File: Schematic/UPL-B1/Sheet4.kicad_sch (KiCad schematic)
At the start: 61 parts, among them P40 TestPoint

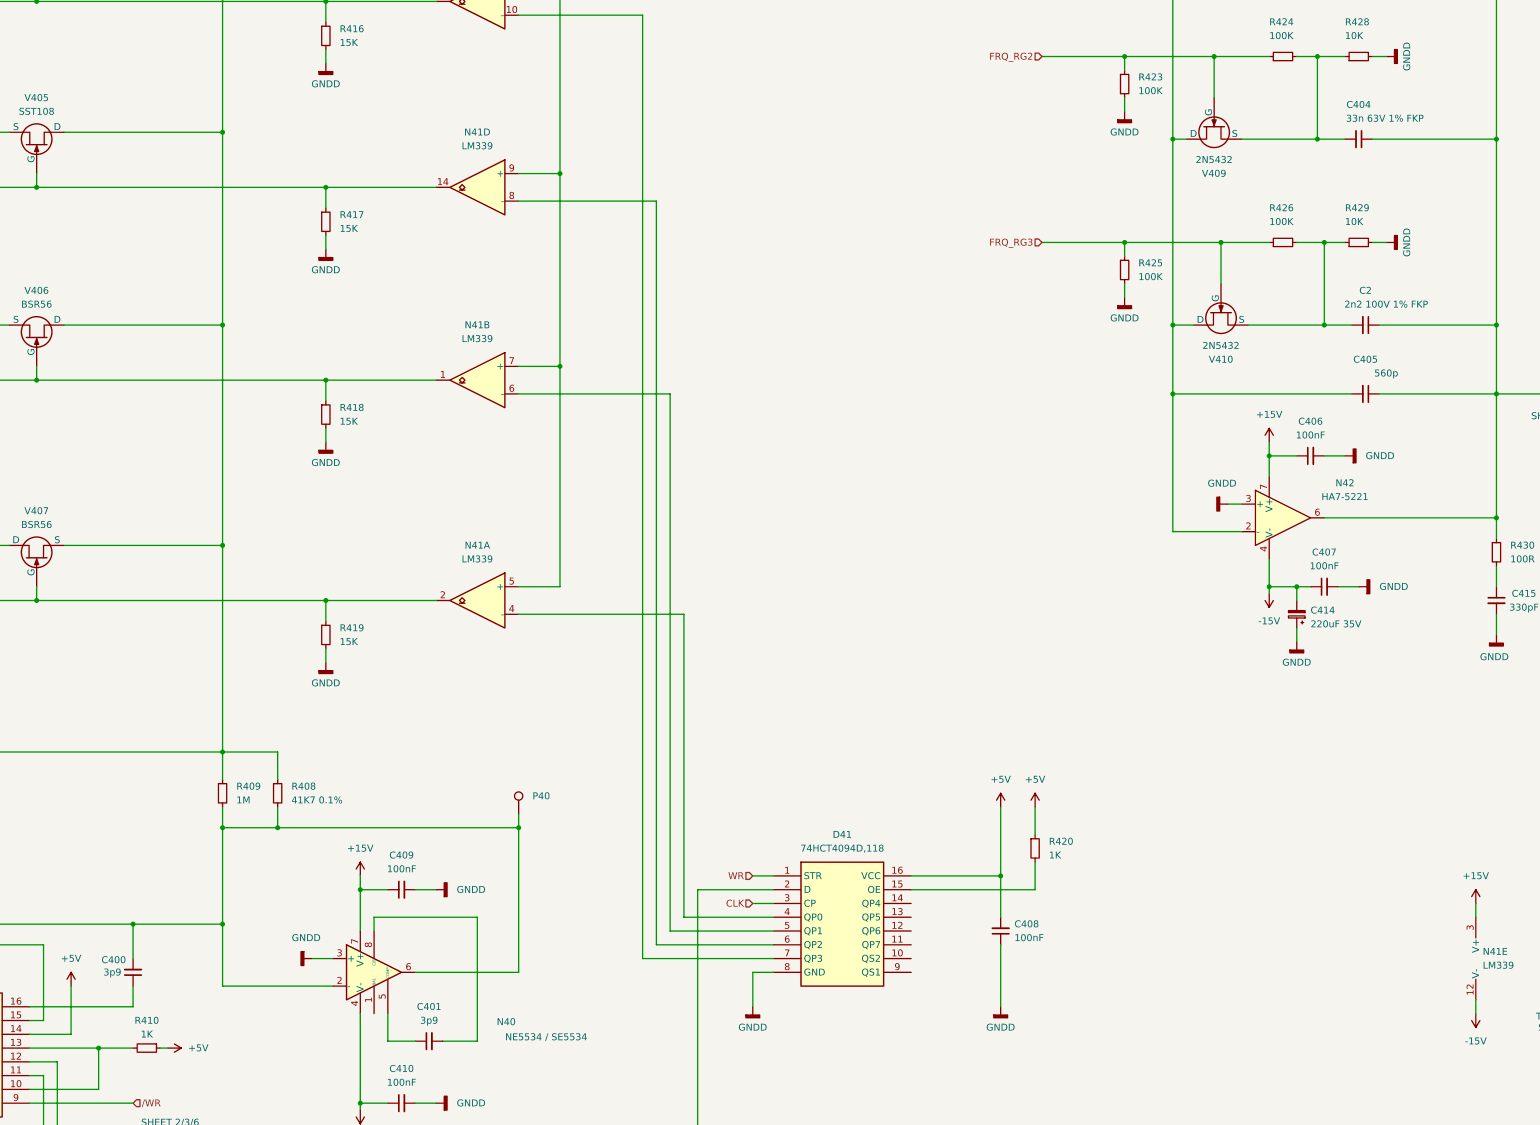
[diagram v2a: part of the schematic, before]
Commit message: Cleanup component names
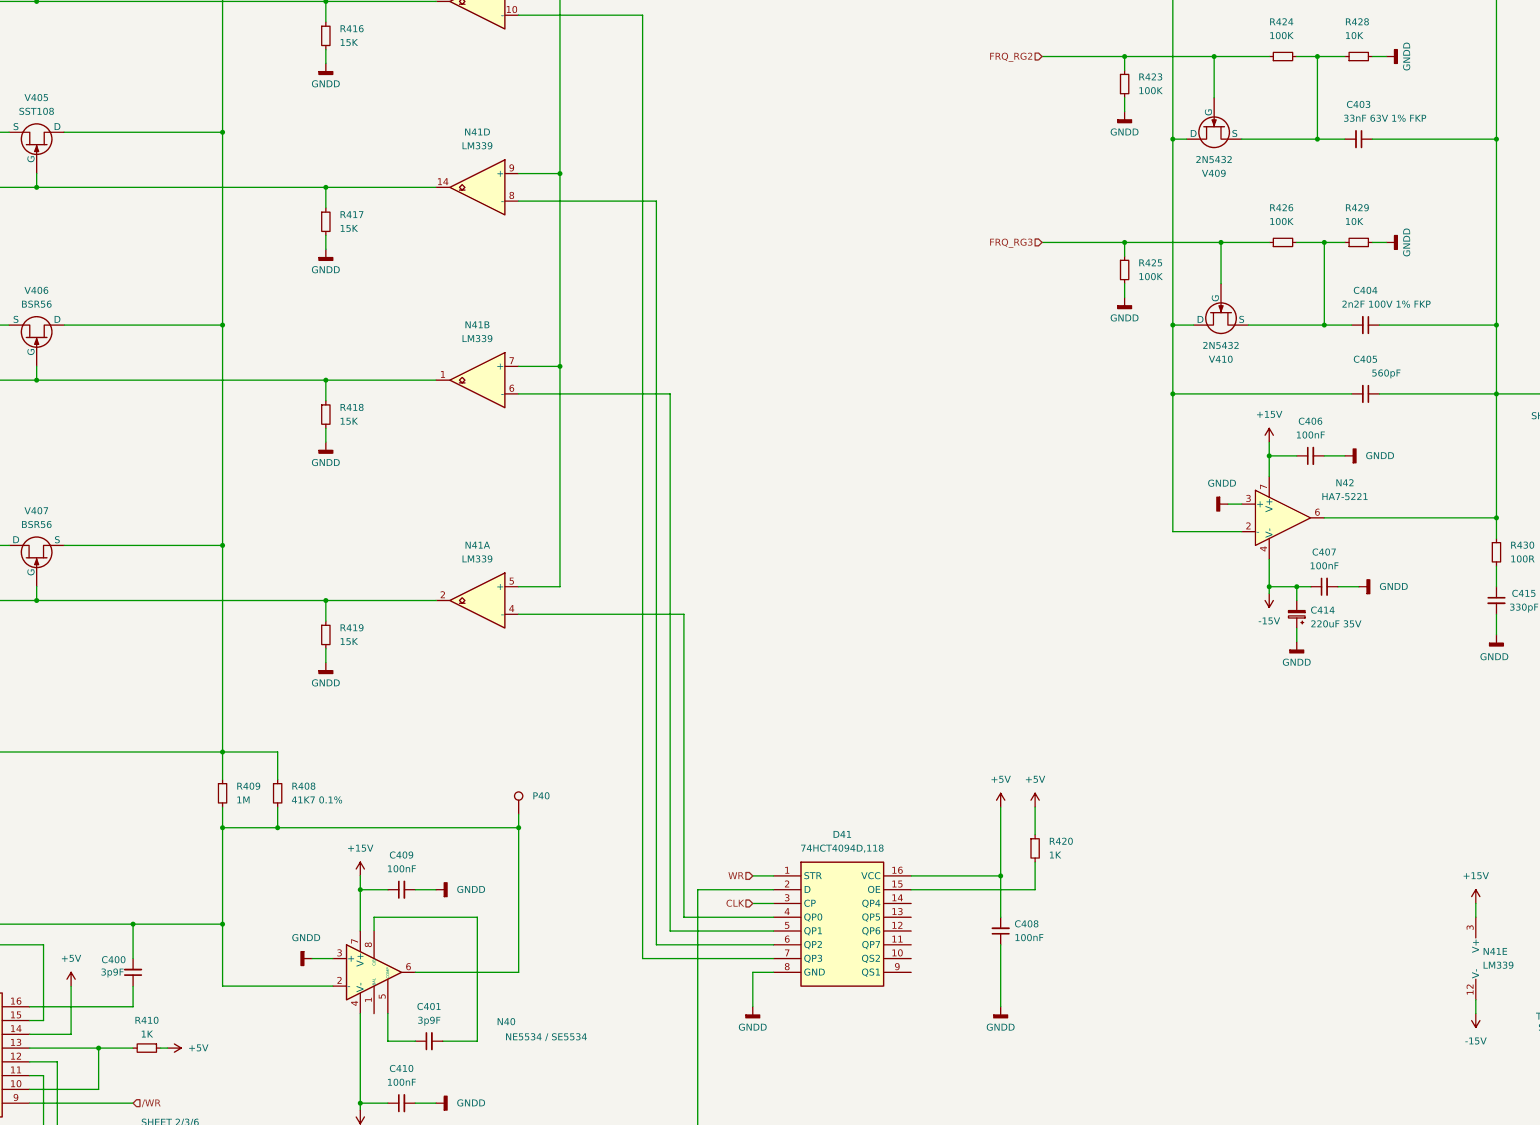
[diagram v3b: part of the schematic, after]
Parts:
- C400, C401: value 3p9 -> 3p9F
- C403: renamed from C404; value 33n 63V 1% FKP -> 33nF 63V 1% FKP
- C404: renamed from C2; value 2n2 100V 1% FKP -> 2n2F 100V 1% FKP
- C405: value 560p -> 560pF
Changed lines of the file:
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@@
 		(on_board yes)
 		(dnp no)
-		(property "Reference" "C404"
+		(property "Reference" "C403"
 			(at 354.3236 68.58 90)
 			(effects
@@
 			)
 		)
-		(property "Value" "33n 63V 1% FKP"
+		(property "Value" "33nF 63V 1% FKP"
 			(at 359.156 71.12 90)
 			(effects
@@
 			(project "UPL_B1"
 				(path "/812de09b-8b67-463d-bf96-bb3aeeb1ed8d/5c1faa4b-2306-4f0f-97e7-c76d1ee80adb"
-					(reference "C404")
+					(reference "C403")
 					(unit 1)
 				)
@@
 			)
 		)
-		(property "Value" "3p9"
+		(property "Value" "3p9F"
 			(at 182.8863 237.49 90)
 			(effects
@@
 			)
 		)
-		(property "Value" "3p9"
+		(property "Value" "3p9F"
 			(at 124.46 228.5937 0)
 			(effects
@@
 		(on_board yes)
 		(dnp no)
-		(property "Reference" "C2"
+		(property "Reference" "C404"
 			(at 355.5936 102.87 90)
 			(effects
@@
 			)
 		)
-		(property "Value" "2n2 100V 1% FKP"
+		(property "Value" "2n2F 100V 1% FKP"
 			(at 359.41 105.41 90)
 			(effects
@@
 			(project "UPL_B1"
 				(path "/812de09b-8b67-463d-bf96-bb3aeeb1ed8d/5c1faa4b-2306-4f0f-97e7-c76d1ee80adb"
-					(reference "C2")
+					(reference "C404")
 					(unit 1)
 				)
@@
 			)
 		)
-		(property "Value" "560p"
+		(property "Value" "560pF"
 			(at 359.41 118.11 90)
 			(effects

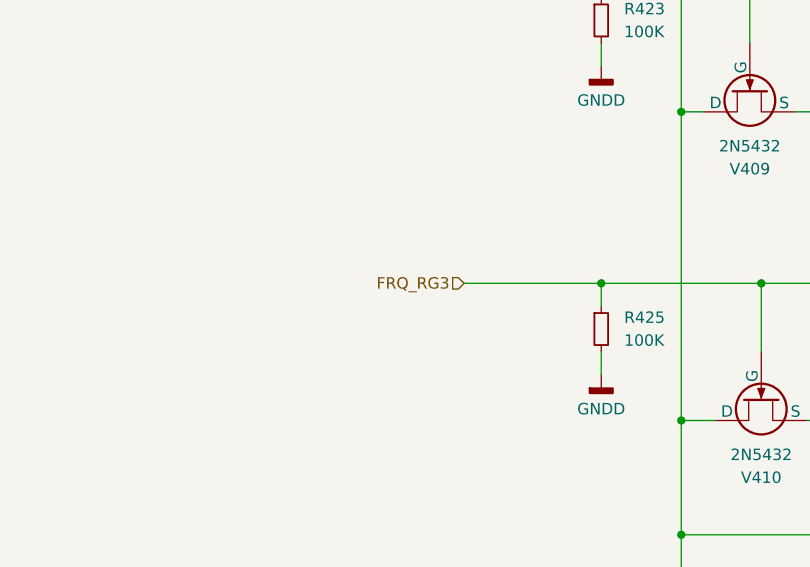
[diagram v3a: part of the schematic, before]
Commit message: Redraw block diagram as vector art. Add more links in hierarchical overview.
Remove original picture
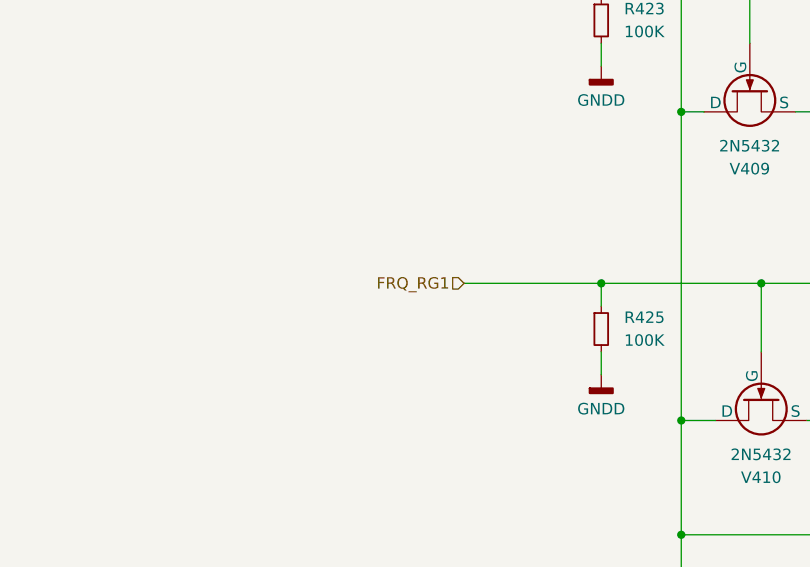
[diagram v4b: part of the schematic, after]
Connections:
- net FRQ_RG3: no longer R425.1, R426.1, V410.2 (G)
- new net FRQ_RG1: R425.1, R426.1, V410.2 (G)
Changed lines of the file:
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@@
 		)
 	)
-	(hierarchical_label "FRQ_RG3"
+	(hierarchical_label "FRQ_RG1"
 		(shape input)
 		(at 295.91 93.98 180)

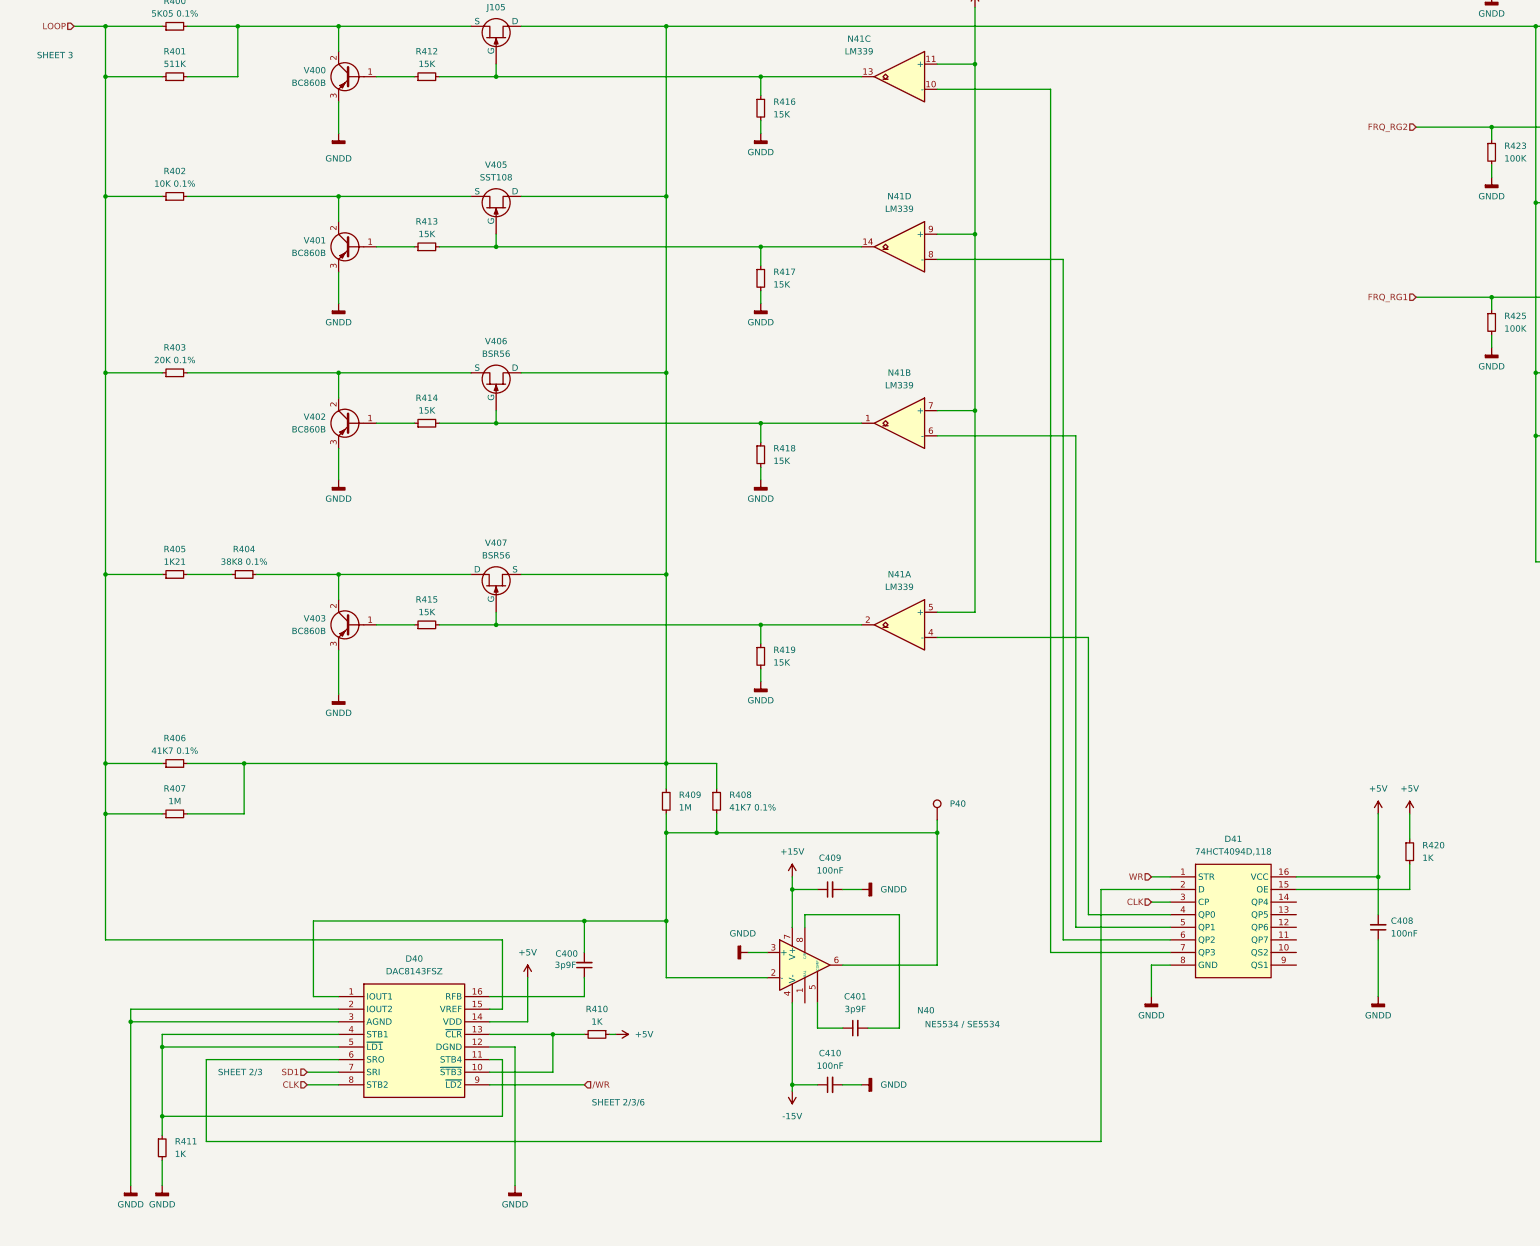
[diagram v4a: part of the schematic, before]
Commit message: Updated symbols for ADC and Shiftregister
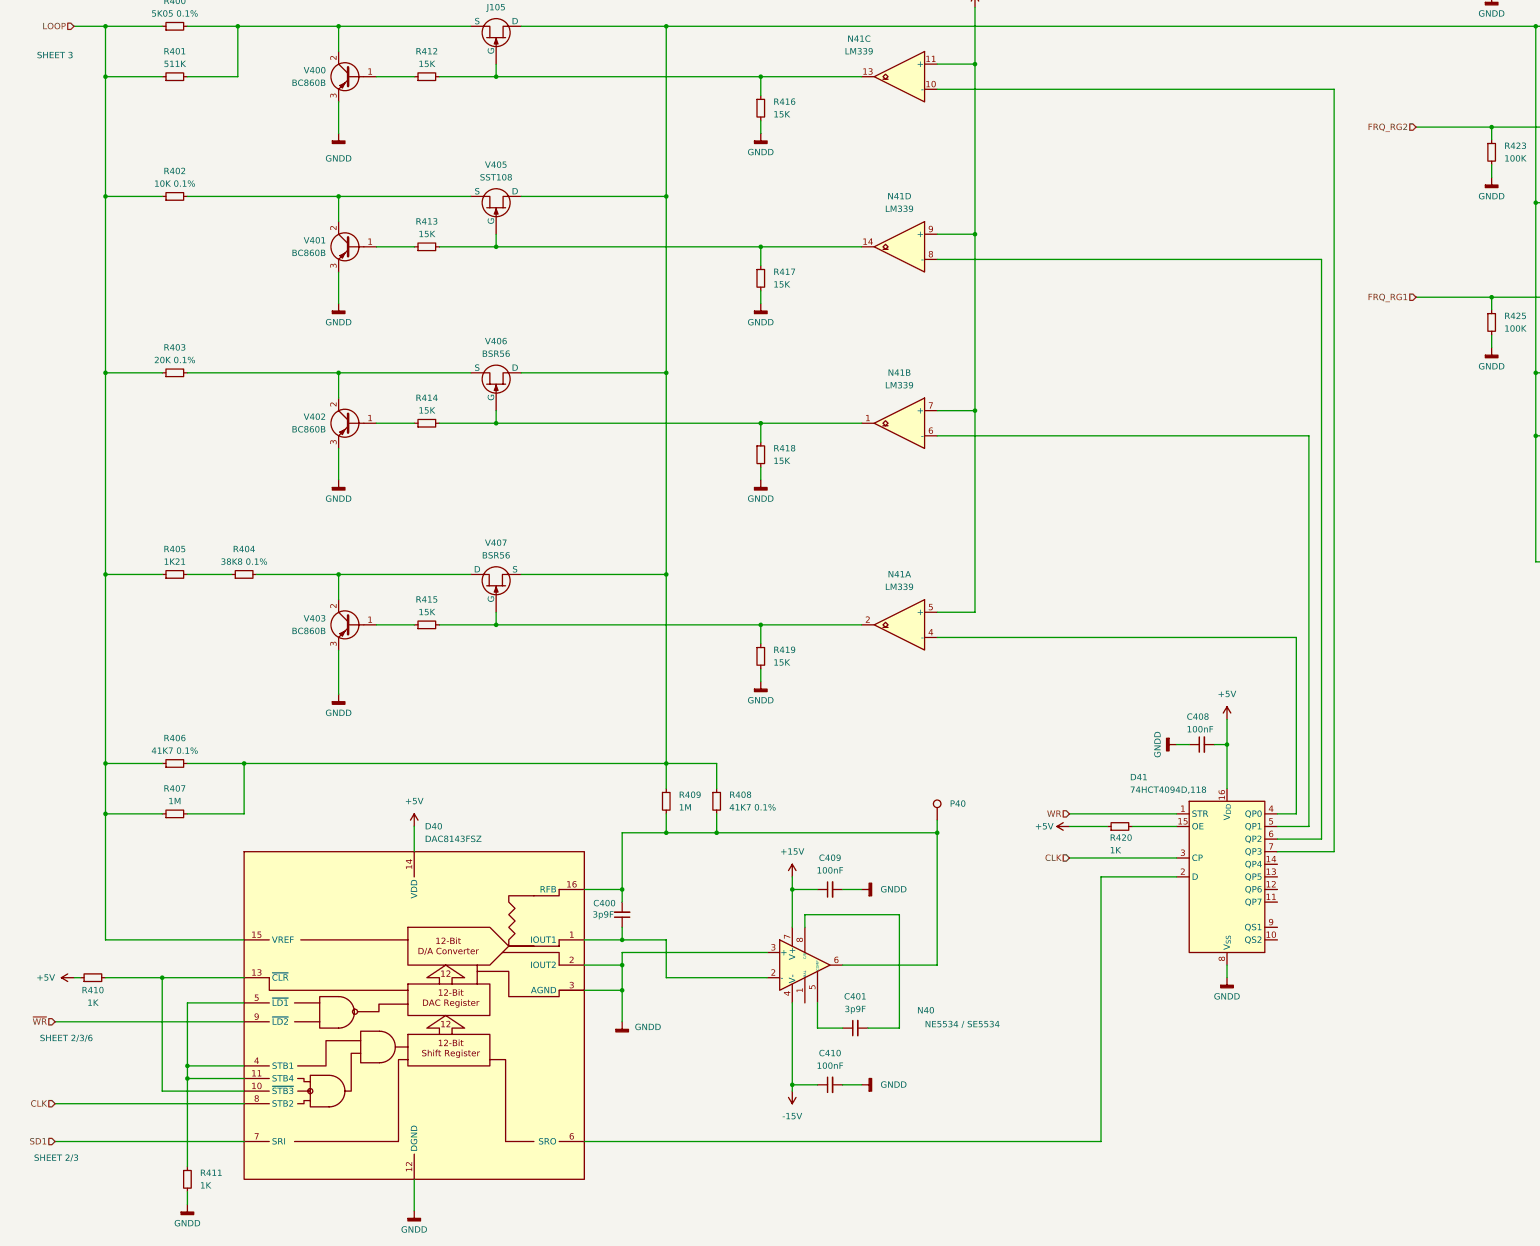
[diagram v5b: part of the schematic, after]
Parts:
- D40: symbol UPL_B1:DAC8143FSZ -> UPL_B1:DAC8143FSZ_
- D41: footprint 74HCT4094D118 -> Package_SO:SOIC-16_3.9x9.9mm_P1.27mm; symbol UPL_B1:74HCT4094D,118 -> UPL_B1:74HCT4094T-L
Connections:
- net at C400.2, N40.6, P40.1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: now also D40.16 (RFB); no longer D40.1 (IOUT1), N40.2 (-)
- net at C400.1: now also D40.1 (IOUT1), N40.2 (-); no longer D40.16 (RFB)
- net /WR renamed ~{WR}
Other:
- moved on the sheet: C400, C408, D41, R410, R411, R420

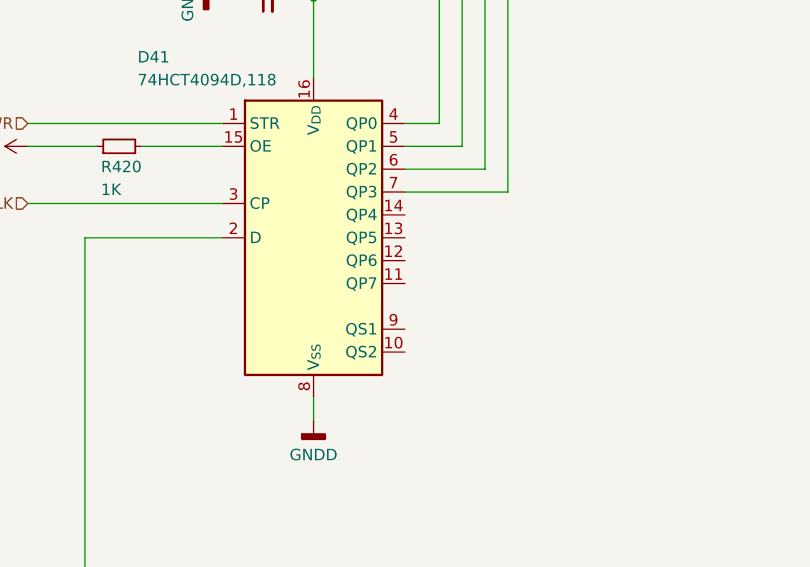
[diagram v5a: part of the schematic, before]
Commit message: Group functional blocks in ALC. Begin documenting digital chain.
Fixed D21 designator, placed a few NC-Crosses on unused pins for good
practice.
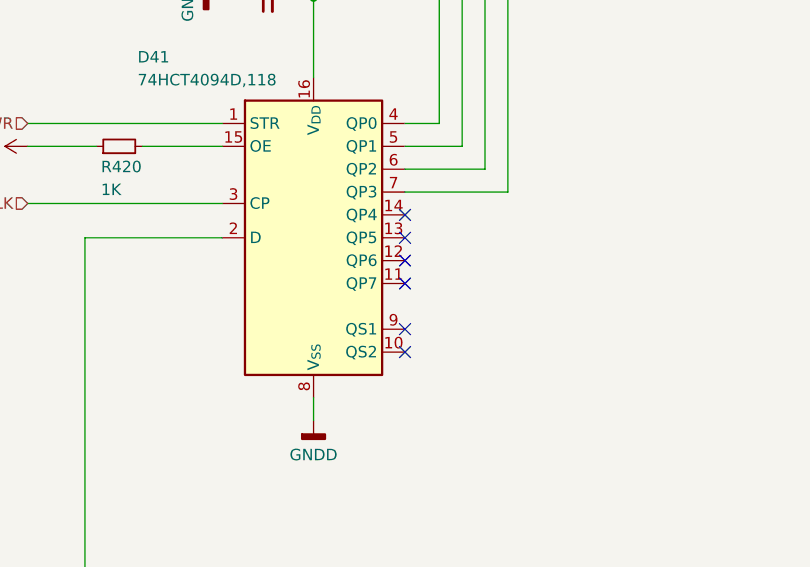
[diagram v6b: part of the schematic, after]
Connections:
- no-connect marks 0 -> 6
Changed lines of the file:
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@@
 		(color 0 0 0 0)
+	)
+	(no_connect
+		(at 267.97 210.82)
+	)
+	(no_connect
+		(at 267.97 215.9)
+	)
+	(no_connect
+		(at 267.97 223.52)
+	)
+	(no_connect
+		(at 267.97 213.36)
+	)
+	(no_connect
+		(at 267.97 220.98)
+	)
+	(no_connect
+		(at 267.97 208.28)
 	)
 	(wire
